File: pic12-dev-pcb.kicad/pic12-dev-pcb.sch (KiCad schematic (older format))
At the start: 11 parts, among them J1 PGM-Conn, J2 App-Conn1, J3 App-Conn2, J4 Conn_SR, J6 Conn_BB1, U1 PIC12F675-ISN

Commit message: Rev5: added GP3 to connectors
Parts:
- J2: footprint Connector_PinHeader_2.54mm:PinHeader_1x07_P2.54mm_Vertical -> Connector_PinHeader_2.54mm:PinHeader_1x08_P2.54mm_Vertical; symbol Connector:Conn_01x07_Male -> Connector:Conn_01x08_Male
- J3: footprint Connector_PinHeader_2.54mm:PinHeader_2x07_P2.54mm_Vertical -> Connector_PinHeader_2.54mm:PinHeader_2x08_P2.54mm_Vertical; symbol Connector_Generic:Conn_02x07_Odd_Even -> Connector_Generic:Conn_02x08_Odd_Even
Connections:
- net +5V: now also J2.6 (Pin_6), J3.11 (Pin_11), J3.12 (Pin_12); no longer J2.5 (Pin_5), J3.10 (Pin_10), J3.9 (Pin_9)
- net GND: now also J2.5 (Pin_5), J3.10 (Pin_10), J3.9 (Pin_9); no longer J2.4 (Pin_4), J3.7 (Pin_7), J3.8 (Pin_8)
- net GP4: now also J2.7 (Pin_7), J3.13 (Pin_13), J3.14 (Pin_14); no longer J2.6 (Pin_6), J3.11 (Pin_11), J3.12 (Pin_12)
- net GP5: now also J2.8 (Pin_8), J3.15 (Pin_15), J3.16 (Pin_16); no longer J2.7 (Pin_7), J3.13 (Pin_13), J3.14 (Pin_14)
- net GP3: now reaches J1.5 (Pin_5), U1.4 (GP3)
- net GP3: now also J2.4 (Pin_4), J3.7 (Pin_7), J3.8 (Pin_8)
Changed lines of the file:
@@
 Sheet 1 1
 Title "PIC12-Development Breadboard-PCB"
-Date "2020-10-28"
-Rev "4"
+Date "2020-10-30"
+Rev "5"
 Comp "Bernhard Bablok"
 Comment1 "https://github.com/bablokb/pcb-pic-devboard"
@@
 $EndComp
 $Comp
-L Connector:Conn_01x07_Male J2
+L Connector:Conn_01x08_Male J2
 U 1 1 5F04965B
 P 8050 3600
 F 0 "J2" H 8350 2950 50  0000 R CNN
 F 1 "App-Conn1" H 8350 3050 50  0000 R CNN
-F 2 "Connector_PinHeader_2.54mm:PinHeader_1x07_P2.54mm_Vertical" H 8050 3600 50  0001 C CNN
+F 2 "Connector_PinHeader_2.54mm:PinHeader_1x08_P2.54mm_Vertical" H 8050 3600 50  0001 C CNN
 F 3 "~" H 8050 3600 50  0001 C CNN
 	1    8050 3600
@@
 Text Notes 4250 3300 2    63   ~ 0
 Vpp\nVdd\nGND\nGP0/DAT\nGP1/CLK
+Text Label 7850 3200 2    50   ~ 0
+GP5
 Text Label 7850 3300 2    50   ~ 0
-GP5
+GP4
 Text Label 7850 3400 2    50   ~ 0
-GP4
++5V
 Text Label 7850 3500 2    50   ~ 0
-+5V
-Text Label 7850 3600 2    50   ~ 0
 GND
 Text Label 7850 3900 2    50   ~ 0
@@
 Connection ~ 4950 3550
 $Comp
-L Connector_Generic:Conn_02x07_Odd_Even J3
+L Connector_Generic:Conn_02x08_Odd_Even J3
 U 1 1 5F4BCD54
 P 8700 3600
 F 0 "J3" H 8800 2950 50  0000 R CNN
 F 1 "App-Conn2" H 9000 3050 50  0000 R CNN
-F 2 "Connector_PinHeader_2.54mm:PinHeader_2x07_P2.54mm_Vertical" H 8700 3600 50  0001 C CNN
+F 2 "Connector_PinHeader_2.54mm:PinHeader_2x08_P2.54mm_Vertical" H 8700 3600 50  0001 C CNN
 F 3 "~" H 8700 3600 50  0001 C CNN
 	1    8700 3600
 	1    0    0    1
 $EndComp
-Text Label 8500 3300 2    50   ~ 0
-GP5
-Text Label 8500 3400 2    50   ~ 0
-GP4
-Text Label 8500 3500 2    50   ~ 0
-+5V
-Text Label 8500 3600 2    50   ~ 0
-GND
 Text Label 8500 3900 2    50   ~ 0
 GP0
@@
 Wire Wire Line
 	6600 2950 6850 2950
-Text Label 9000 3300 0    50   ~ 0
-GP5
-Text Label 9000 3400 0    50   ~ 0
-GP4
-Text Label 9000 3500 0    50   ~ 0
-+5V
-Text Label 9000 3600 0    50   ~ 0
-GND
 Text Label 9000 3900 0    50   ~ 0
 GP0
@@
 Wire Wire Line
 	5150 3650 4250 3650
+Text Label 8500 3500 2    50   ~ 0
+GND
+Text Label 8500 3400 2    50   ~ 0
++5V
+Text Label 8500 3300 2    50   ~ 0
+GP4
+Text Label 8500 3200 2    50   ~ 0
+GP5
+Text Label 9000 3200 0    50   ~ 0
+GP5
+Text Label 9000 3300 0    50   ~ 0
+GP4
+Text Label 9000 3400 0    50   ~ 0
++5V
+Text Label 9000 3500 0    50   ~ 0
+GND
+Text Label 9000 3600 0    50   ~ 0
+GP3
+Text Label 8500 3600 2    50   ~ 0
+GP3
+Text Label 7850 3600 2    50   ~ 0
+GP3
+Text Label 6800 3450 0    50   ~ 0
+GP3
+Wire Wire Line
+	6500 3450 6800 3450
+Connection ~ 6500 3450
 $EndSCHEMATC

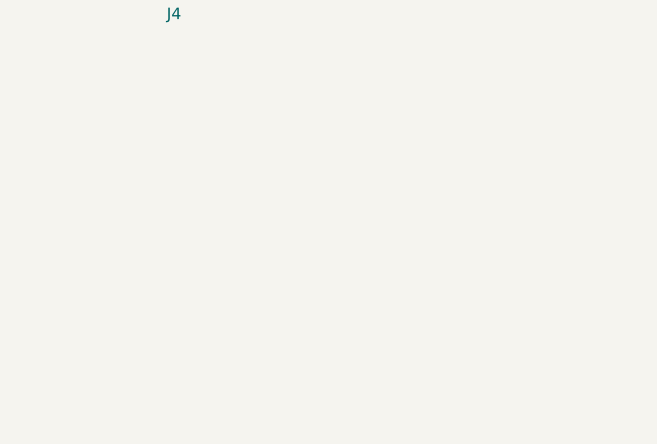
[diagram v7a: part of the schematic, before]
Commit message: Rev6: added LEDs and button
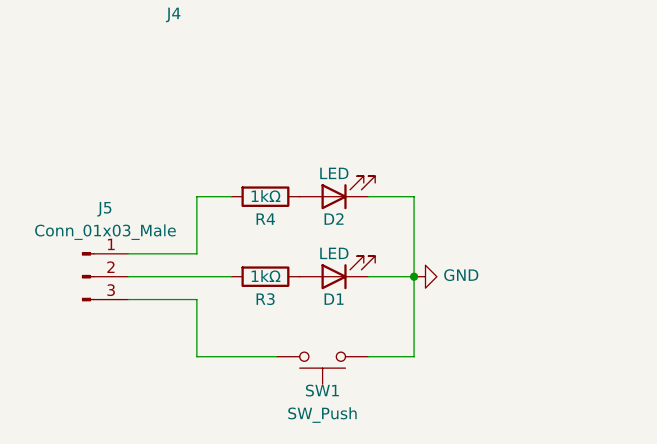
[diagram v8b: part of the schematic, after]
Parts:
- added D1, D2: LED, LED_SMD:LED_1206_3216Metric_Pad1.42x1.75mm_HandSolder, symbol Device:LED
- added J5: Conn_01x03_Male, Connector_PinHeader_2.54mm:PinHeader_1x03_P2.54mm_Vertical, symbol Connector:Conn_01x03_Male
- added R3, R4: 1kΩ, Resistor_SMD:R_1206_3216Metric_Pad1.30x1.75mm_HandSolder, symbol Device:R
- added SW1: SW_Push, user:SW_PUSH_SLIM_1x4, symbol Switch:SW_Push
- J6: footprint Connector_PinHeader_2.54mm:PinHeader_1x02_P2.54mm_Horizontal -> Connector_PinHeader_2.54mm:PinHeader_1x02_P2.54mm_Vertical
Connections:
- net GND: now also D1.1 (K), D2.1 (K), SW1.2
- new net: D1.2 (A), R3.1
- new net: J5.2 (Pin_2), R3.2
- new net: J5.1 (Pin_1), R4.2
- new net: J5.3 (Pin_3), SW1.1
- new net: D2.2 (A), R4.1
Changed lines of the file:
@@
 Title "PIC12-Development Breadboard-PCB"
 Date "2020-10-30"
-Rev "5"
+Rev "6"
 Comp "Bernhard Bablok"
 Comment1 "https://github.com/bablokb/pcb-pic-devboard"
@@
 F 0 "J6" H 4700 5300 50  0000 C CNN
 F 1 "Conn_BB1" H 4700 5150 50  0000 C CNN
-F 2 "Connector_PinHeader_2.54mm:PinHeader_1x02_P2.54mm_Horizontal" H 4600 5000 50  0001 C CNN
+F 2 "Connector_PinHeader_2.54mm:PinHeader_1x02_P2.54mm_Vertical" H 4600 5000 50  0001 C CNN
 F 3 "~" H 4600 5000 50  0001 C CNN
 	1    4600 5000
@@
 	6500 3450 6800 3450
 Connection ~ 6500 3450
+$Comp
+L Device:R R3
+U 1 1 5F9D00BF
+P 2750 4950
+F 0 "R3" V 2850 4950 50  0000 C CNN
+F 1 "1kΩ" V 2750 4950 50  0000 C CNN
+F 2 "Resistor_SMD:R_1206_3216Metric_Pad1.30x1.75mm_HandSolder" V 2680 4950 50  0001 C CNN
+F 3 "~" H 2750 4950 50  0001 C CNN
+	1    2750 4950
+	0    1    1    0
+$EndComp
+$Comp
+L Connector:Conn_01x03_Male J5
+U 1 1 5F9D134F
+P 1950 4950
+F 0 "J5" H 2050 5250 50  0000 C CNN
+F 1 "Conn_01x03_Male" H 2050 5150 50  0000 C CNN
+F 2 "Connector_PinHeader_2.54mm:PinHeader_1x03_P2.54mm_Vertical" H 1950 4950 50  0001 C CNN
+F 3 "~" H 1950 4950 50  0001 C CNN
+	1    1950 4950
+	1    0    0    -1
+$EndComp
+$Comp
+L Device:LED D1
+U 1 1 5F9D1E69
+P 3050 4950
+F 0 "D1" H 3050 5050 50  0000 C CNN
+F 1 "LED" H 3050 4850 50  0000 C CNN
+F 2 "LED_SMD:LED_1206_3216Metric_Pad1.42x1.75mm_HandSolder" H 3050 4950 50  0001 C CNN
+F 3 "~" H 3050 4950 50  0001 C CNN
+	1    3050 4950
+	-1   0    0    1
+$EndComp
+$Comp
+L Switch:SW_Push SW1
+U 1 1 5F9D3FD3
+P 3000 5300
+F 0 "SW1" H 3000 5450 50  0000 C CNN
+F 1 "SW_Push" H 3000 5550 50  0000 C CNN
+F 2 "user:SW_PUSH_SLIM_1x4" H 3000 5500 50  0001 C CNN
+F 3 "~" H 3000 5500 50  0001 C CNN
+	1    3000 5300
+	1    0    0    1
+$EndComp
+$Comp
+L power:GND #PWR01
+U 1 1 5F9D46D7
+P 3400 4950
+F 0 "#PWR01" H 3400 4700 50  0001 C CNN
+F 1 "GND" V 3405 4822 50  0000 R CNN
+F 2 "" H 3400 4950 50  0001 C CNN
+F 3 "" H 3400 4950 50  0001 C CNN
+	1    3400 4950
+	0    -1   -1   0
+$EndComp
+Wire Wire Line
+	2150 5050 2450 5050
+Wire Wire Line
+	2450 5050 2450 5300
+Wire Wire Line
+	2450 5300 2800 5300
+$Comp
+L Device:R R4
+U 1 1 5F9EC54C
+P 2750 4600
+F 0 "R4" V 2850 4600 50  0000 C CNN
+F 1 "1kΩ" V 2750 4600 50  0000 C CNN
+F 2 "Resistor_SMD:R_1206_3216Metric_Pad1.30x1.75mm_HandSolder" V 2680 4600 50  0001 C CNN
+F 3 "~" H 2750 4600 50  0001 C CNN
+	1    2750 4600
+	0    1    1    0
+$EndComp
+$Comp
+L Device:LED D2
+U 1 1 5F9EC552
+P 3050 4600
+F 0 "D2" H 3050 4700 50  0000 C CNN
+F 1 "LED" H 3050 4500 50  0000 C CNN
+F 2 "LED_SMD:LED_1206_3216Metric_Pad1.42x1.75mm_HandSolder" H 3050 4600 50  0001 C CNN
+F 3 "~" H 3050 4600 50  0001 C CNN
+	1    3050 4600
+	-1   0    0    1
+$EndComp
+Wire Wire Line
+	2450 4600 2600 4600
+Wire Wire Line
+	3200 4600 3400 4600
+Wire Wire Line
+	3400 4600 3400 4950
+Wire Wire Line
+	3200 5300 3400 5300
+Connection ~ 3400 4950
+Wire Wire Line
+	3400 4950 3400 5300
+Wire Wire Line
+	3200 4950 3400 4950
+Wire Wire Line
+	2150 4950 2600 4950
+Wire Wire Line
+	2450 4600 2450 4850
+Wire Wire Line
+	2450 4850 2150 4850
 $EndSCHEMATC
